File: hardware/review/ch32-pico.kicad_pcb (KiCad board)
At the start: 4 copper layers, 21 x 51 mm, 52 parts, among them J1 PICO 40-PIN, J2 GT-USB-7010AW, SW1 RESET, SW2 BOOT, U1 CH32X035C8T6, U4 AP63203WU-7

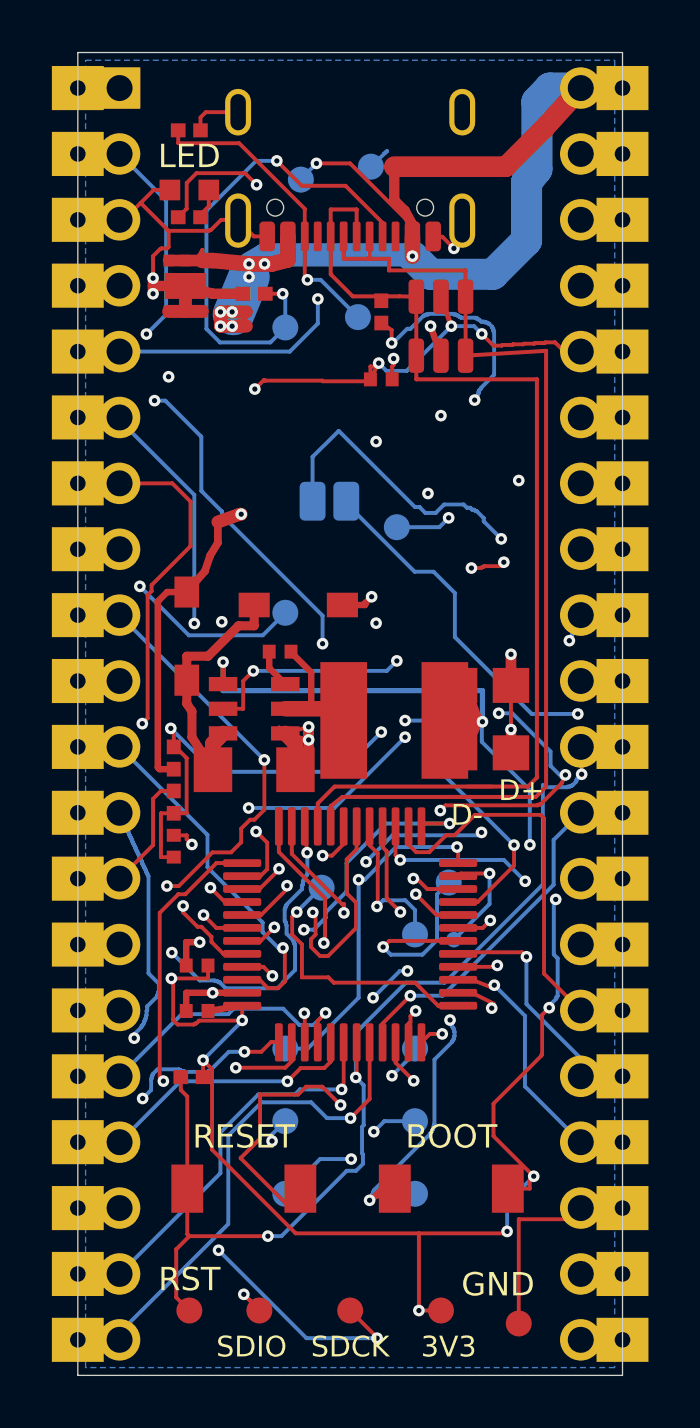
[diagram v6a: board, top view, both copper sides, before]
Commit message: Move the regulator under USB-C and centre the MCU
The 3.3 V buck, its diode-OR inputs and the VBUS sense divider now sit in
the band directly below the connector, beside header pins 36, 37 and 39
that they serve, instead of mid-board where the removed load switch used
to leave room for them. The MCU moves to the fanout's reference position
at y = 28 mm so both header columns and the USB pair reach it with similar
lengths, with decoupling and the reset pull-up following it. SJ1 and the
USB probe contacts move with the shortened USB tail.

The board is rerouted from the new seed with the pinned Freerouting run;
a locked back-layer feed reaches the VBUS probe pad that routers strand in
the ground pour. Vias drop from 141 to 115 and trace length from 1368 to
1219 mm, with no signal on the ground layer. Five stitching vias are
re-planned for the new copper. DRC, connectivity, geometry audits, tests,
the routing patch, panel, fabrication bundle and renders are regenerated.
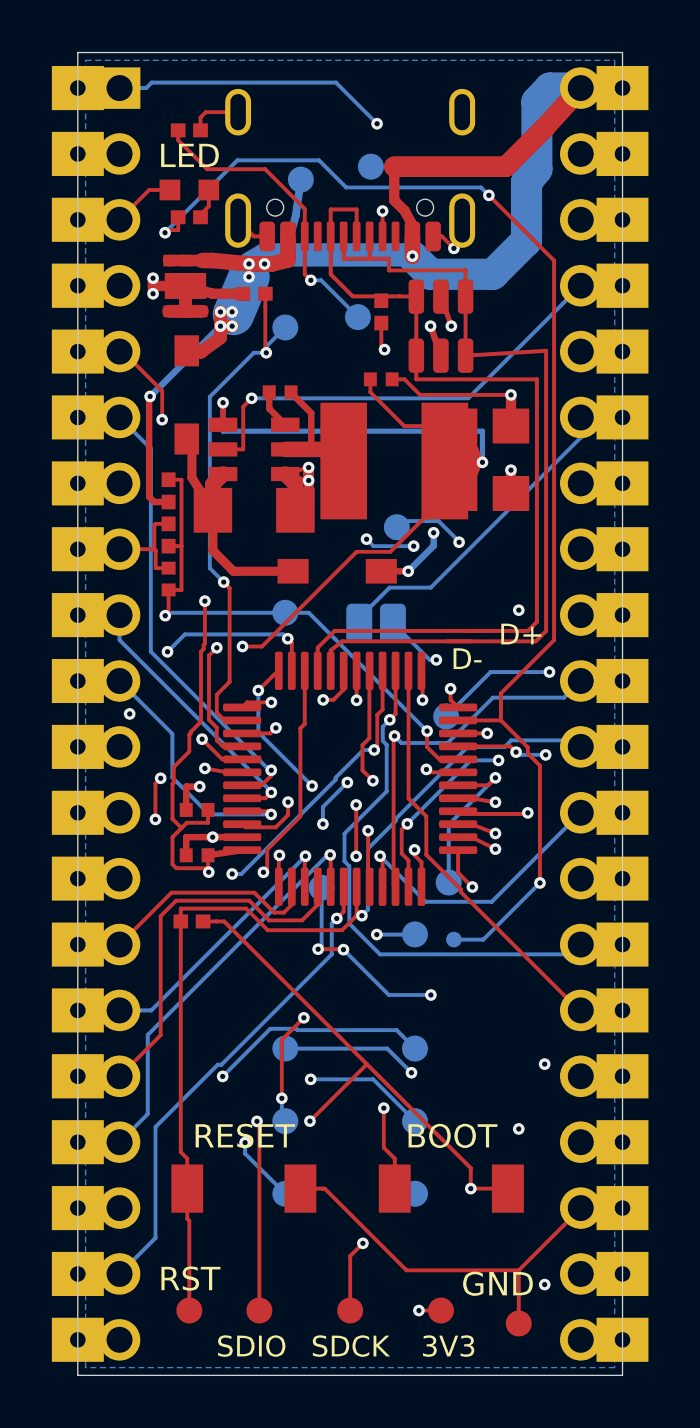
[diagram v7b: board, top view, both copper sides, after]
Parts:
- moved C9 10.3 mm to (3.50, 20.3)
- moved R1 10.3 mm to (3.50, 16.9)
- moved R2 10.3 mm to (3.50, 18.6)
- moved C4 10.0 mm to (7.80, 13.1)
- moved C1 10.0 mm to (6.80, 17.6)
- moved C3 10.0 mm to (15.7, 17.0)
- moved L1 10.0 mm to (12.2, 15.8)
- moved U4 10.0 mm to (6.80, 15.3)
- moved C2 10.00 mm to (15.7, 14.4)
- moved D1 9.30 mm to (4.20, 13.2)
- moved C6 6.00 mm to (4.60, 30.9)
- moved C7 6.00 mm to (4.60, 29.2)
- moved R10 6.00 mm to (4.40, 33.5)
- moved TP23 6.00 mm to (15.5, 22.3)
- moved TP24 6.00 mm to (14.7, 22.7)
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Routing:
- net 3V3_OUT: track 101.9 -> 74.8 mm, vias 15 -> 9
- net PB12: track 13.5 -> 32.4 mm, vias 2 -> 5
- net VBUS: track 79.7 -> 60.9 mm, vias 10 -> 9
- net VBUS_SENSE: track 37.8 -> 20.8 mm, vias 4 -> 2
- net PA9: track 34.4 -> 18.2 mm
- net PC7: track 24.2 -> 8.01 mm
- net PB2: track 26.2 -> 11.8 mm, vias 4 -> 2
- net PB5: track 18.9 -> 33.1 mm, vias 3 -> 7
- net BOOT_PULLUP: track 45.3 -> 34.1 mm, vias 4 -> 2
- net PA2: track 29.2 -> 18.3 mm, vias 3 -> 1
- net PA15: track 19.0 -> 8.23 mm, vias 3 -> 1
- net PA1: track 24.7 -> 14.1 mm, vias 5 -> 2
- net PB7: track 9.85 -> 20.3 mm, vias 2 -> 1
- net PA6: track 17.9 -> 27.4 mm
- net 3V3_EN: track 26.8 -> 17.4 mm, vias 2 -> 1
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
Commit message: Lock a 3.3 V supply trunk, widen VSYS and stitch the back pour
The 3.3 V inner pour was split into islands by signal routing and the MCU's
island hung off 0.15 mm router taps. A locked 0.6 mm trunk on the supply
layer now joins the regulator output to a via at the MCU decoupling
capacitor and to header pin 36, and the rerouted pour is one polygon. VSYS
runs at 0.4 mm. The stitch planner may now place vias through the wide part
of the 3.3 V pour, so 17 grid vias keep every point of the back pour within
6 mm of a ground via or pin. Rerouted with the pinned Freerouting run; DRC,
connectivity, geometry audits, tests, patch, bundle and renders regenerated.
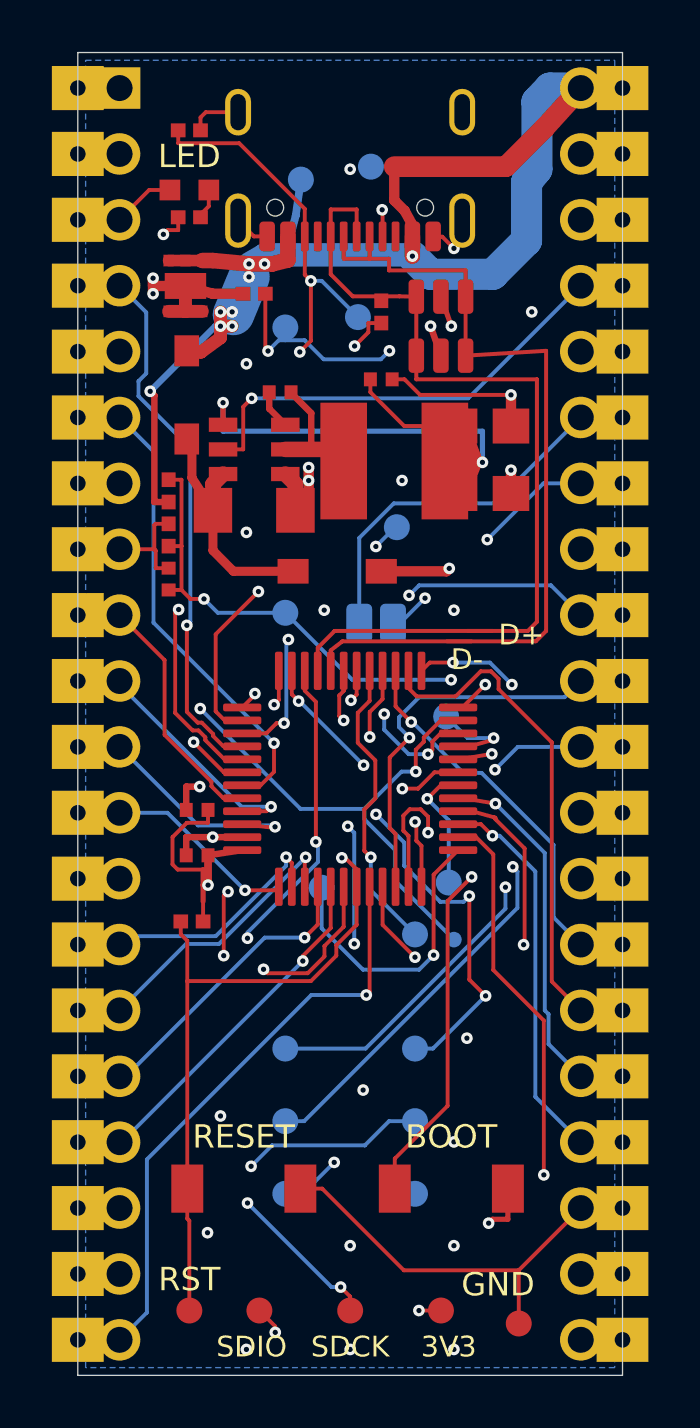
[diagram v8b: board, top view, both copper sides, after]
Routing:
- net PB12: track 32.4 -> 20.2 mm
- net STATUS_LED: track 50.1 -> 40.0 mm
- net PA1: track 14.1 -> 22.4 mm
- net PB5: track 33.1 -> 25.2 mm, vias 7 -> 3
- net PB1: track 11.5 -> 3.70 mm, vias 3 -> 1
- net PB10: track 36.1 -> 28.8 mm, vias 2 -> 1
- net BOOT_PULLUP: track 34.1 -> 41.2 mm
- net PB7: track 20.3 -> 14.0 mm
- net PB13: track 22.3 -> 27.5 mm, vias 3 -> 4
- net PA6: track 27.4 -> 23.2 mm
- net GND: track 52.6 -> 48.6 mm, vias 15 -> 27
- net PC7: track 8.01 -> 11.8 mm
- net PA14: track 12.0 -> 8.57 mm
- net PA22: track 26.0 -> 22.7 mm
- net PB6: track 15.9 -> 18.9 mm
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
